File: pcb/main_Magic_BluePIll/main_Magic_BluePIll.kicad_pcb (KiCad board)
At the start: 2 copper layers, 95.3 x 113.2 mm, 56 parts, among them J1 PW, J10 ESC1, J11 ESC2, J12 ESC3, J14 UART_Out, J2 MPU6050, J4 LiPo, J9 Sensors, SW1 Power_SW, SW2 EN_Push, SW3 Boot_Push, SW4 BUTTON_Push, U1 ESP32-WROOM-32E, U6 CN3903

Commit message: bluepill pcb
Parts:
- removed the ? at (88.8, 174.9)
- removed the ? at (134.2, 160.8)
- removed the ? at (65.6, 178.7)
- removed C24, C6: 100nF, Capacitor_SMD:C_0805_2012Metric
- removed C7: 1uF, Capacitor_SMD:C_0805_2012Metric
- removed C8: 100nF, Capacitor_SMD:C_0603_1608Metric
- removed ESC_3: TerminalBlock_Phoenix_PT-1,5-3-3.5-H_1x03_P3.50mm_Horizontal, TerminalBlock_Phoenix:TerminalBlock_Phoenix_PT-1,5-3-3.5-H_1x03_P3.50mm_Horizontal
- removed H5, H6: M3, MountingHole:MountingHole_3mm
- removed J10: ESC1, Connector_JST:JST_XH_S2B-XH-A_1x02_P2.50mm_Horizontal
- removed J11: ESC2, Connector_JST:JST_XH_S2B-XH-A_1x02_P2.50mm_Horizontal
- removed J12: ESC3, Connector_JST:JST_XH_S2B-XH-A_1x02_P2.50mm_Horizontal
- removed J14: UART_Out, Connector_JST:JST_XH_S4B-XH-A_1x04_P2.50mm_Horizontal
- removed JP1: ESP_JP, Resistor_SMD:R_1206_3216Metric
- removed JP2: LED_JP, Resistor_SMD:R_1206_3216Metric
- removed SW3: Boot_Push, MixLib:SW_Push_SPST_NO_Alps_SKRK_Handsolder
- added ?: , , F.Cu at (92.7, 235.8)
- added D5: LED_ON, MixLib:LED_0805_2012Metric, F.Cu at (36.6, 165.7)
- added D7: SS14, Diode_SMD:D_SMA, F.Cu at (74.2, 251.8)
- added J3: ST_Link, Connector_PinHeader_2.54mm:PinHeader_1x05_P2.54mm_Vertical, F.Cu at (79.6, 235.2)
- added J5: ESC, Connector_JST:JST_XH_B6B-XH-A_1x06_P2.50mm_Vertical, F.Cu at (121.2, 234.4)
- added Q1: IRLML2502, Package_TO_SOT_SMD:SOT-23, F.Cu at (36.9, 161.9)
- added R10: 470, Resistor_SMD:R_0805_2012Metric, F.Cu at (32.3, 164.0)
- added R11: 470, Resistor_SMD:R_0805_2012Metric, F.Cu at (32.3, 166.9)
- added R12: 470, Resistor_SMD:R_0805_2012Metric, F.Cu at (32.3, 169.9)
- added R13: 1k, Resistor_SMD:R_0603_1608Metric, F.Cu at (36.5, 168.4)
- added R8: 330, Resistor_SMD:R_0805_2012Metric, F.Cu at (32.3, 161.0)
- added U2: AMS1117CD-3.3, Package_TO_SOT_SMD:TO-252-3_TabPin2, F.Cu at (37.0, 155.5)
- added U3: HC05, MixLib:HC05, F.Cu at (71.0, 157.4)
- D2: value WS2812B -> LED_RGB; footprint LED_SMD:LED_WS2812B_PLCC4_5.0x5.0mm_P3.2mm -> LED_SMD:LED_RGB_5050-6
- D3: value WS2812B -> SS14; footprint LED_SMD:LED_WS2812B_PLCC4_5.0x5.0mm_P3.2mm -> Diode_SMD:D_SMA
- D4: value LED_ON -> LED_SW
- H11, H12: value M3 -> M2; footprint MountingHole:MountingHole_3mm -> MountingHole:MountingHole_2.2mm_M2
- R1: value 330 -> 10k
- R2: value 10k -> 1k; footprint Resistor_SMD:R_0603_1608Metric -> Resistor_SMD:R_1206_3216Metric
- R3: value 10k -> 330k; footprint Resistor_SMD:R_0603_1608Metric -> Resistor_SMD:R_1206_3216Metric
- R4: value 330 -> 100k; footprint Resistor_SMD:R_0805_2012Metric -> Resistor_SMD:R_1206_3216Metric
- R5: value 330 -> 1k; footprint Resistor_SMD:R_0805_2012Metric -> Resistor_SMD:R_1206_3216Metric
- SW1: footprint Button_Switch_THT:SW_Push_2P2T_Toggle_CK_PVA2OAH5xxxxxxV2 -> Button_Switch_SMD:SW_DPDT_CK_JS202011JCQN
- SW2: value EN_Push -> PUSH_2; footprint MixLib:SW_Push_SPST_NO_Alps_SKRK_Handsolder -> MixLib:SW_Push_Sw-3424p_Handsolder
- SW4: value BUTTON_Push -> PUSH_1; footprint Button_Switch_SMD:SW_SPST_CK_RS282G05A3 -> MixLib:SW_Push_Sw-3424p_Handsolder
- U1: value ESP32-WROOM-32E -> BluePill_SWD_Breakout; footprint PCM_Espressif:ESP32-WROOM-32E -> MixLib:BluePill_SWD
- U6: value CN3903 -> CN3905
- moved R1 153.6 mm to (52.5, 264.9), turned to 0 degrees
- moved SW1 135.2 mm to (-14.7, 149.9)
- moved SW2 119.0 mm to (47.0, 265.6), turned to 0 degrees
- moved U6 114.5 mm to (-16.5, 166.6)
- moved C2 112.6 mm to (30.7, 214.9)
- moved C28 112.6 mm to (23.2, 219.3)
- moved D1 112.6 mm to (13.7, 214.2)
- moved J4 112.6 mm to (16.1, 219.9)
- moved D4 112.3 mm to (-25.8, 160.9)
- moved R7 112.3 mm to (-25.7, 163.6)
- moved D3 111.1 mm to (74.2, 247.2), turned to 0 degrees
- moved H11 106.7 mm to (89.0, 130.7)
- moved H12 106.7 mm to (124.0, 130.7)
- moved U1 82.7 mm to (114.1, 235.6), turned to 180 degrees
- moved D6 73.4 mm to (14.8, 178.6)
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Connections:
- BZ1 pad 1: /BUZ -> Net-(BZ1-+)
- C3 pad 1: /VDD_ESP -> +3.3V
- C4 pad 1: /VDD_ESP -> +3.3V
- D2 pad 1: Net-(D2-VDD) -> GND
- D2 pad 2: /D_LED2 -> GND
- D2 pad 4: /D_LED1 -> Net-(D2-BA)
- D3 pad 1: Net-(D3-VDD) -> +5V
- D3 pad 2: /D_LED1 -> Net-(D3-A)
- D4 pad 2: +3.3V -> +5V
- J4 pad 1: /VM -> unconnected-(J4-Pin_1-Pad1)
- J4 pad 2: GND -> unconnected-(J4-Pin_2-Pad2)
- R1 pad 1: Net-(D2-VDD) -> GND
- R1 pad 2: +3.3V -> /PUSH_2
- R2 pad 1: /EN -> Net-(BZ1-+)
- R2 pad 2: +3.3V -> /Vb
- R3 pad 1: /BOOT -> /Vb
- R3 pad 2: +3.3V -> Net-(R3-Pad2)
- R4 pad 1: Net-(BZ1--) -> Net-(R3-Pad2)
- R5 pad 1: Net-(D3-VDD) -> /V_bat
- R5 pad 2: +3.3V -> Net-(R3-Pad2)
- R9 pad 2: /BUTTON -> /PUSH_1
- SW2 pad 1: /EN -> +3.3V
- SW2 pad 2: GND -> /PUSH_2
- SW4 pad 2: /BUTTON -> /PUSH_1
- U1 pad 1: GND -> unconnected-(U1-PB12-Pad1)
- U1 pad 10: /ESC_1 -> unconnected-(U1-PA15-Pad10)
- U1 pad 11: /BUZ -> unconnected-(U1-PB3-Pad11)
- U1 pad 12: /Data_2aux -> unconnected-(U1-PB4-Pad12)
- U1 pad 13: /LED_BLUE -> unconnected-(U1-PB5-Pad13)
- U1 pad 14: /LED_RGB -> unconnected-(U1-PB6-Pad14)
- U1 pad 15: GND -> unconnected-(U1-PB7-Pad15)
- U1 pad 16: /Data_1aux -> unconnected-(U1-PB8-Pad16)
- U1 pad 19: unconnected-(U1-NC-Pad19) -> GND
- U1 pad 2: /VDD_ESP -> unconnected-(U1-PB13-Pad2)
- U1 pad 20: unconnected-(U1-NC-Pad20) -> +3.3V
- U1 pad 23: /Data_SIG -> unconnected-(U1-PC14-Pad23)
- U1 pad 24: /Data_S3 -> unconnected-(U1-PC15-Pad24)
- U1 pad 25: /BOOT -> unconnected-(U1-PA0-Pad25)
- U1 pad 27: /Data_S2 -> unconnected-(U1-PA2-Pad27)
- U1 pad 28: /Data_S1 -> unconnected-(U1-PA3-Pad28)
- U1 pad 3: /EN -> unconnected-(U1-PB14-Pad3)
- U1 pad 30: /Data_S0 -> unconnected-(U1-PA5-Pad30)
- U1 pad 31: /Data_EN -> unconnected-(U1-PA6-Pad31)
- U1 pad 33: /SDA -> unconnected-(U1-PB0-Pad33)
- U1 pad 34: /TX -> unconnected-(U1-PB1-Pad34)
- U1 pad 35: /RX -> unconnected-(U1-PB10-Pad35)
- U1 pad 36: /SCL -> unconnected-(U1-PB11-Pad36)
- U1 pad 37: /BUTTON -> /RST
- U1 pad 38: GND -> +3.3V
- U1 pad 4: /Enc1 -> unconnected-(U1-PB15-Pad4)
- U1 pad 5: /Enc2 -> unconnected-(U1-PA8-Pad5)
- U1 pad 6: /CurrESC1&2 -> unconnected-(U1-PA9-Pad6)
- U1 pad 7: /CurrESC2 -> unconnected-(U1-PA10-Pad7)
- U1 pad 8: /ESC_3 -> unconnected-(U1-PA11-Pad8)
- U1 pad 9: /ESC_2 -> unconnected-(U1-PA12-Pad9)
- U6 pad 3: +3.3V -> Net-(D3-A)
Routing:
- net +3.3V: track 265.0 -> 6.83 mm, vias 4 -> 0
- net /RX: track 114.1 -> 0.00 mm, vias 1 -> 0
- net /TX: track 109.6 -> 0.00 mm, vias 1 -> 0
- net /Data_2aux: track 96.9 -> 0.00 mm
- net /VM: track 95.1 -> 0.00 mm
- net /SCL: track 91.8 -> 0.00 mm, vias 1 -> 0
- net /Data_1aux: track 88.8 -> 0.00 mm
- net /SDA: track 87.7 -> 0.00 mm, vias 1 -> 0
- net /SWIO: track 0.00 -> 73.2 mm
- net /SWCLK: track 0.00 -> 66.8 mm
- net /BUZ: track 62.6 -> 0.00 mm, vias 1 -> 0
- net /ESC_1: track 57.4 -> 0.00 mm
- net /D_LED1: track 55.3 -> 0.00 mm, vias 2 -> 0
- net /ESC_2: track 51.6 -> 0.00 mm
- net /ESC_3: track 48.9 -> 0.00 mm
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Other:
- outline, holes or cut-outs redrawn
- board text added: "Hacer el agarre de 3 puent3s (no4). Agrandar turbina."

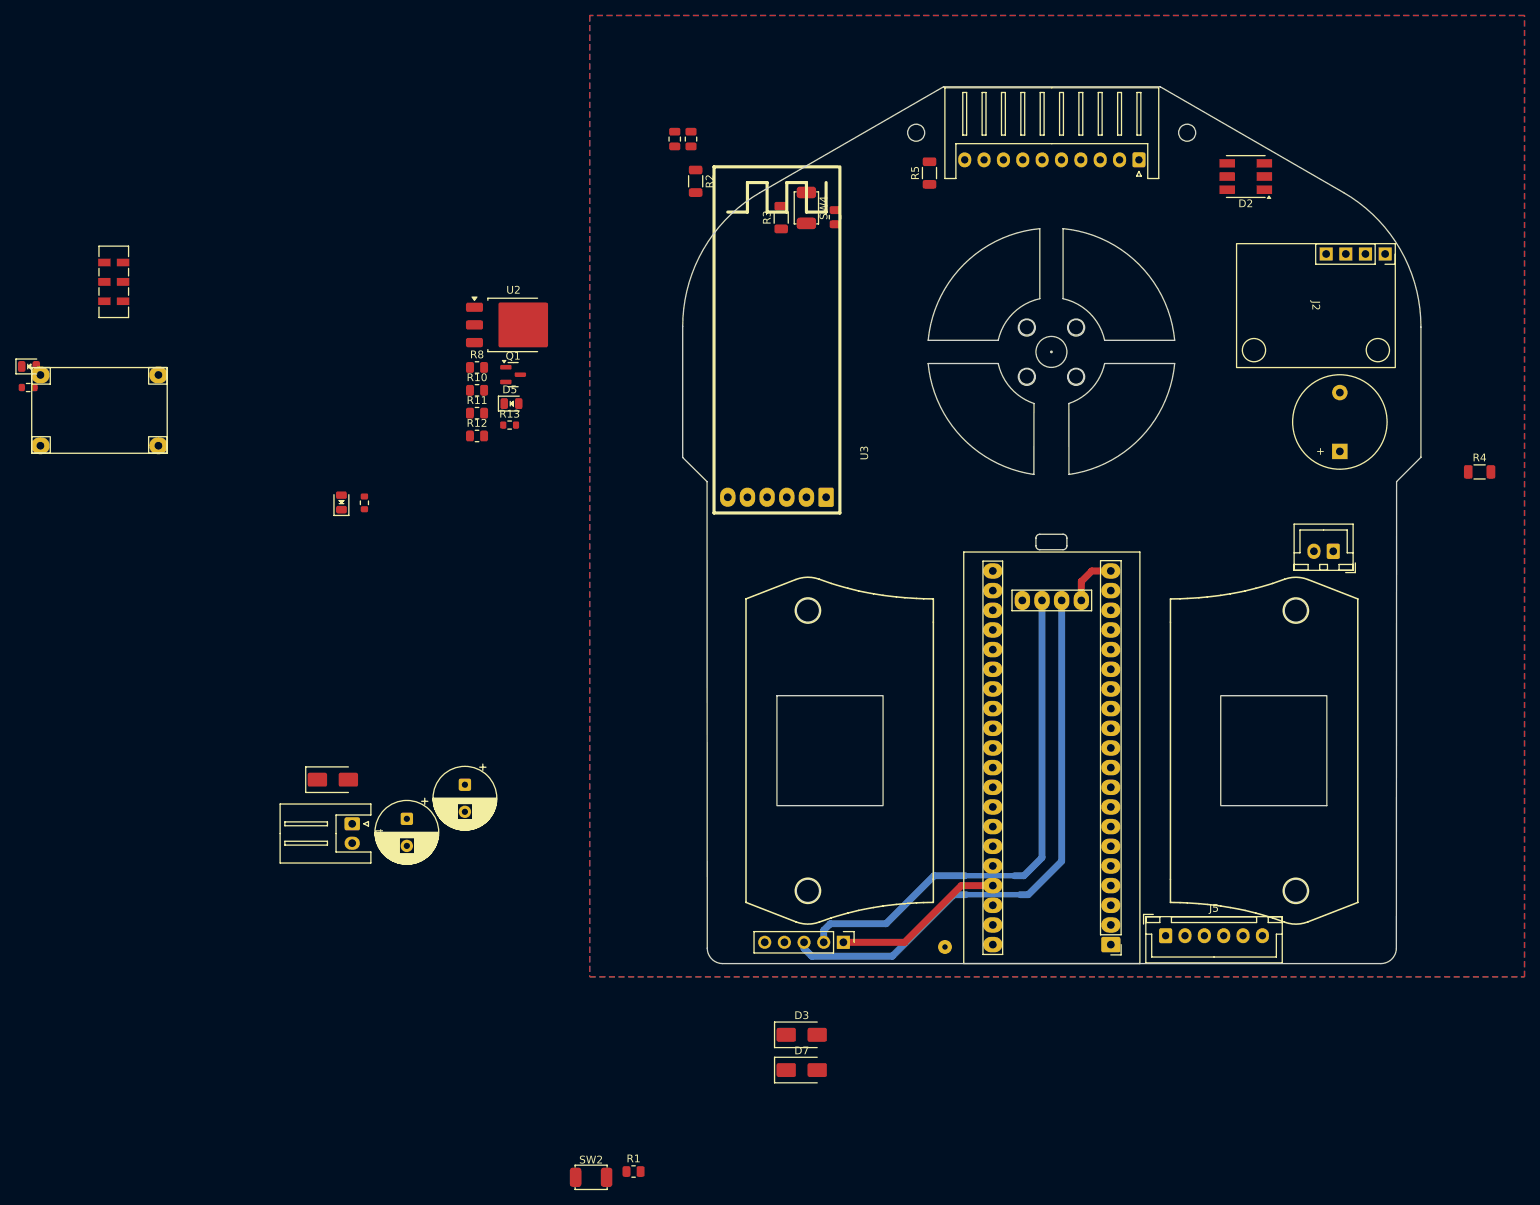
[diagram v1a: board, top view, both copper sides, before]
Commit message: components arranged in bluepill pcb
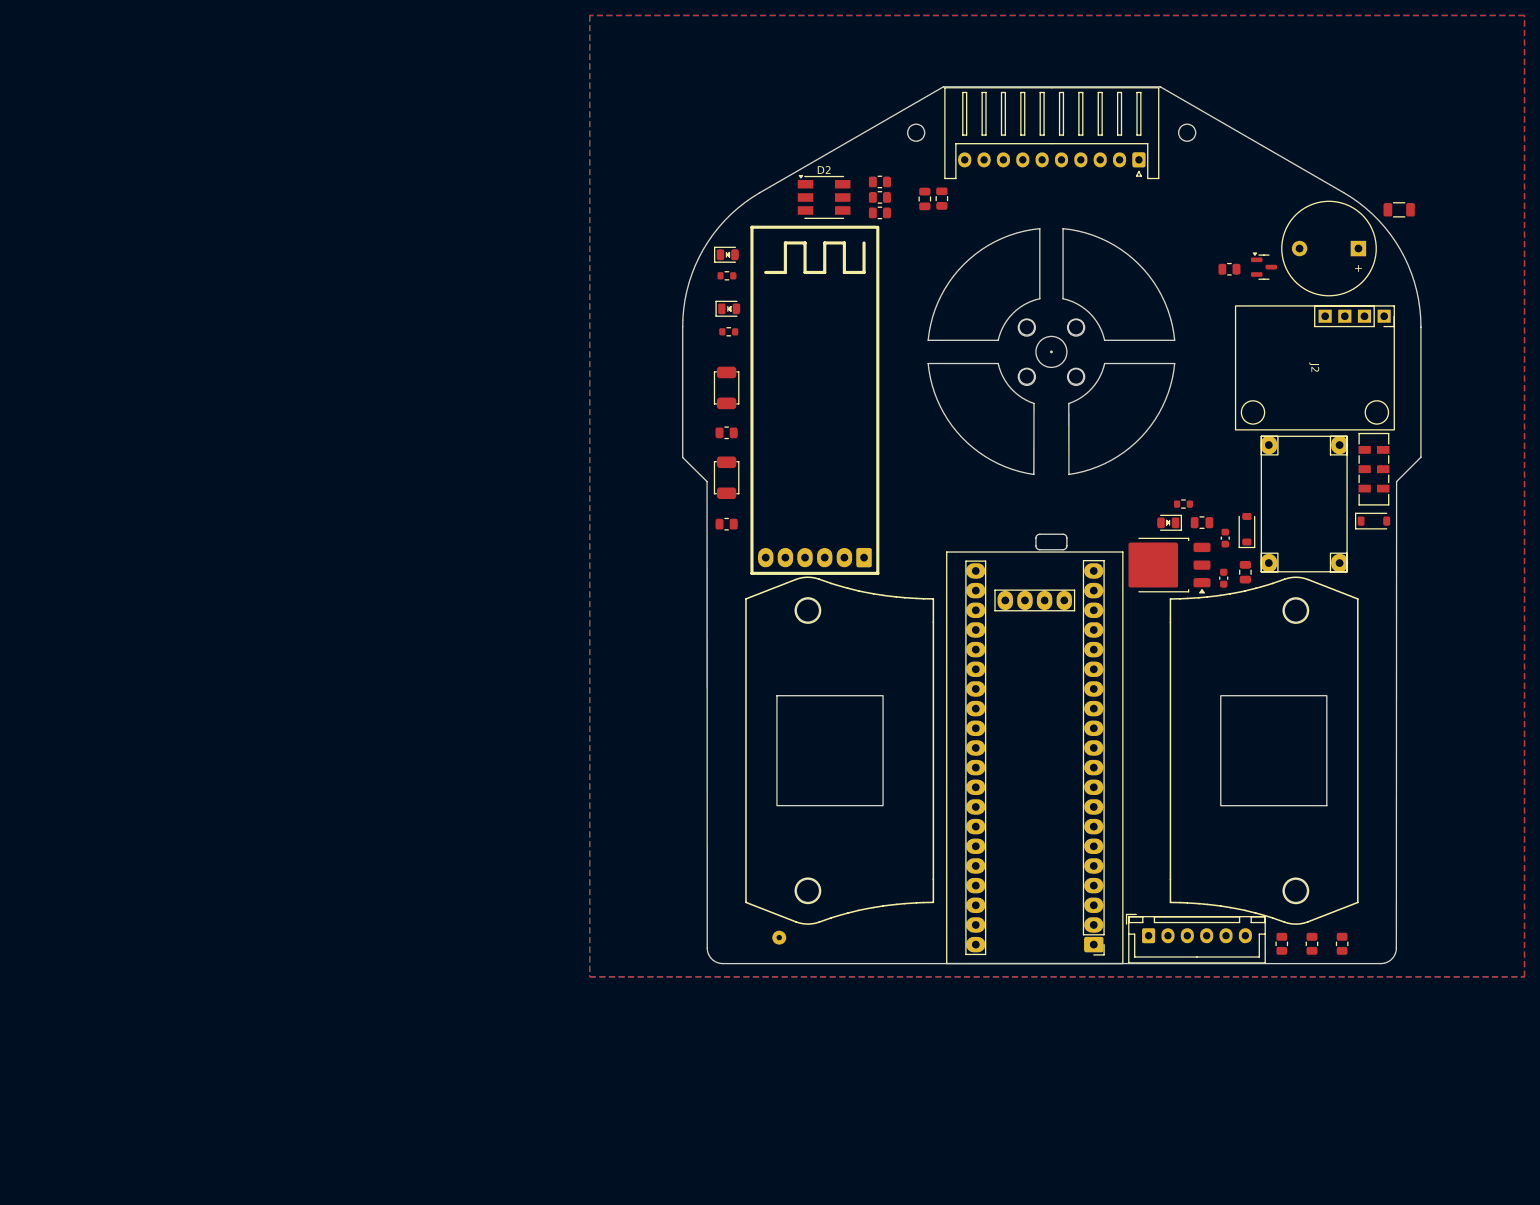
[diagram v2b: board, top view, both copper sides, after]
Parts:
- removed C2: 100uF, Capacitor_THT:CP_Radial_D8.0mm_P3.50mm
- removed C28: 470uF, Capacitor_THT:CP_Radial_D8.0mm_P3.50mm
- removed D7: SS14, Diode_SMD:D_SMA
- removed J1: PW, Connector_JST:JST_XH_B2B-XH-A_1x02_P2.50mm_Vertical
- removed J3: ST_Link, Connector_PinHeader_2.54mm:PinHeader_1x05_P2.54mm_Vertical
- removed J4: LiPo, Connector_JST:JST_XH_S2B-XH-A_1x02_P2.50mm_Horizontal
- added C1: 100nF, Capacitor_SMD:C_0603_1608Metric, F.Cu at (128.9, 183.1)
- added C5: 100nF, Capacitor_SMD:C_0603_1608Metric, F.Cu at (128.7, 188.2)
- added C6: 10uF, Capacitor_SMD:C_0805_2012Metric, F.Cu at (125.9, 181.1)
- added C7: 10uF, Capacitor_SMD:C_0805_2012Metric, F.Cu at (131.5, 187.4)
- C3: value 22uF -> 10UF
- D1, D3: footprint Diode_SMD:D_SMA -> Diode_SMD:D_SOD-123
- D4: value LED_SW -> LED_5V
- D5: value LED_ON -> LED_3V3
- R13: value 1k -> 4.7k
- R2: value 1k -> 100
- R3, R4, R5: footprint Resistor_SMD:R_1206_3216Metric -> Resistor_SMD:R_0805_2012Metric
- moved SW1 164.5 mm to (148.1, 174.2)
- moved U6 156.1 mm to (139.1, 178.7), turned to 90 degrees
- moved D1 138.5 mm to (148.1, 180.8)
- moved R3 113.9 mm to (136.2, 235.4), turned to -90 degrees
- moved R5 112.9 mm to (144.0, 235.4), turned to -90 degrees
- moved SW2 103.4 mm to (64.5, 163.7), turned to -90 degrees
- moved R8 98.0 mm to (129.4, 148.3)
- moved Q1 98.0 mm to (133.9, 148.1)
- moved R1 96.2 mm to (64.5, 169.4), turned to 180 degrees
- moved D4 91.4 mm to (64.5, 146.5)
- moved R7 91.4 mm to (64.5, 149.2)
- moved R2 90.9 mm to (151.4, 140.7), turned to 0 degrees
- moved U2 89.4 mm to (120.9, 186.5), turned to 180 degrees
- moved R13 87.6 mm to (123.5, 178.7)
- moved D3 87.0 mm to (131.7, 181.9), turned to 90 degrees
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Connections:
- R3 pad 1: /Vb -> /VM
- U1 pad 16: unconnected-(U1-PB8-Pad16) -> /SCL
- U1 pad 17: unconnected-(U1-PB9-Pad17) -> /SDA
- U1 pad 6: unconnected-(U1-PA9-Pad6) -> /BL_RX
- U1 pad 7: unconnected-(U1-PA10-Pad7) -> /BL_TX
- U3 pad RXD: unconnected-(U3-PadRXD) -> /BL_RX
- U3 pad TXD: unconnected-(U3-PadTXD) -> /BL_TX
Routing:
- net /SWIO: track 73.2 -> 0.00 mm
- net /SWCLK: track 66.8 -> 0.00 mm
- net /RST: track 22.3 -> 0.00 mm
- net +3.3V: track 6.83 -> 0.00 mm
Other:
- board text added: "Hacer el agarre de 3 puentes (no4). Agrandar turbina."
- board text removed: "Hacer el agarre de 3 puent3s (no4). Agrandar turbina."
